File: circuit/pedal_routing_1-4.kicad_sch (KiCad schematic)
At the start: 4 parts, among them U110 CD4051B, U113 CD4051B, U114 CD4051B, U116 CD4051B

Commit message: Rebuilt bus and matrix.
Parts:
- renumbered U110 to U16, U114 to U17, U113 to U18, U116 to U19
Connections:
- net AGND: no longer U16.4 (X7), U17.4 (X7), U18.4 (X7), U19.4 (X7)
- net Guitar_Out renamed ROW_2
- net Pedal1_Out renamed ROW_3
- net ROW_3: now also U16.15 (X2); no longer U16.13 (X0)
- net Pedal2_Out renamed ROW_4
- net ROW_4: now also U16.12 (X3), U17.12 (X3); no longer U16.15 (X2), U17.13 (X0)
- removed net Pedal3_Out: U16.12 (X3), U17.12 (X3), U18.13 (X0), U19.1 (X4)
- net Pedal4_Out renamed ROW_5
- net ROW_5: now also U19.1 (X4); no longer U19.13 (X0)
- net Pedal7_Out renamed ROW_6
- net Pedal8_Out renamed ROW_7
- net Row2 renamed PEDAL_1_IN
- net Row3 renamed PEDAL_2_IN
- net Row4 renamed PEDAL_3_IN
- net Row5 renamed PEDAL_4_IN
- new net ROW_1: U16.13 (X0), U17.13 (X0), U18.13 (X0), U19.13 (X0)
- new net ROW_8: U16.4 (X7), U17.4 (X7), U18.4 (X7), U19.4 (X7)

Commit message: Hopefully close to finished
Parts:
- added C117, C118, C119, C120, C121, C122, C123, C124: 0.1mF, Capacitor_THT:C_Axial_L3.8mm_D2.6mm_P7.50mm_Horizontal, symbol Device:C_Small
- renumbered U16 to U17, U17 to U18, U18 to U19, U19 to U22
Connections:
- net U7_Q3 is gone; now on net U8_Q0: U17.11 (A)
- net U7_Q4 is gone; now on net U8_Q1: U17.10 (B)
- net U7_Q5 is gone; now on net U8_Q2: U17.9 (C)
- net U7_Q6 is gone; now on net U8_Q3: U18.11 (A)
- net U7_Q7 is gone; now on net U8_Q4: U18.10 (B)
- net +5V: now also C118.2, C120.2, C122.2, C124.2
- net -5V: now also C117.1, C119.1, C121.1, C123.1
- net AGND: now also C117.2, C118.1, C119.2, C120.1, C121.2, C122.1, C123.2, C124.1
- net U8_Q0: no longer U18.9 (C)
- net U8_Q1: no longer U19.11 (A)
- net U8_Q2: no longer U19.10 (B)
- net U8_Q3: no longer U19.9 (C)
- net U8_Q4: no longer U22.11 (A)
- net U8_Q5: now also U18.9 (C); no longer U22.10 (B)
- net U8_Q6: now also U19.11 (A); no longer U22.9 (C)
- net ROW_8 renamed ROW_9
- new net U8_Q7: U19.10 (B)
- new net U9_Q0: U19.9 (C)
- new net U9_Q1: U22.11 (A)
- new net U9_Q2: U22.10 (B)
- new net U9_Q3: U22.9 (C)
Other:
- moved on the sheet: U17, U18, U19

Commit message: Created pdf and made minor readabilty changes.
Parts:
- C117, C118, C119, C120, C121, C122, C123, C124: value 0.1mF -> 0.1uF
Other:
- title: (none) -> ESP332 Guitar Patch Bay
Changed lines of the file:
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@@
 	(generator "eeschema")
 	(generator_version "9.0")
-	(paper "A4")
+	(paper "USLetter")
+	(title_block
+		(title "ESP332 Guitar Patch Bay")
+		(date "2025-05-27")
+		(rev "1")
+	)
 	(text "Pedal 2 Routing"
 		(exclude_from_sim no)
@@
 			)
 		)
-		(property "Value" "0.1mF"
+		(property "Value" "0.1uF"
 			(at 166.3636 31.75 90)
 			(effects
@@
 			)
 		)
-		(property "Value" "0.1mF"
+		(property "Value" "0.1uF"
 			(at 142.2336 80.01 90)
 			(effects
@@
 			)
 		)
-		(property "Value" "0.1mF"
+		(property "Value" "0.1uF"
 			(at 120.6436 118.11 90)
 			(effects
@@
 			)
 		)
-		(property "Value" "0.1mF"
+		(property "Value" "0.1uF"
 			(at 59.6836 80.01 90)
 			(effects
@@
 			)
 		)
-		(property "Value" "0.1mF"
+		(property "Value" "0.1uF"
 			(at 81.2736 33.02 90)
 			(effects
@@
 			)
 		)
-		(property "Value" "0.1mF"
+		(property "Value" "0.1uF"
 			(at 96.5136 165.1 90)
 			(effects
@@
 			)
 		)
-		(property "Value" "0.1mF"
+		(property "Value" "0.1uF"
 			(at 242.5636 30.48 90)
 			(effects
@@
 			)
 		)
-		(property "Value" "0.1mF"
+		(property "Value" "0.1uF"
 			(at 212.0836 77.47 90)
 			(effects

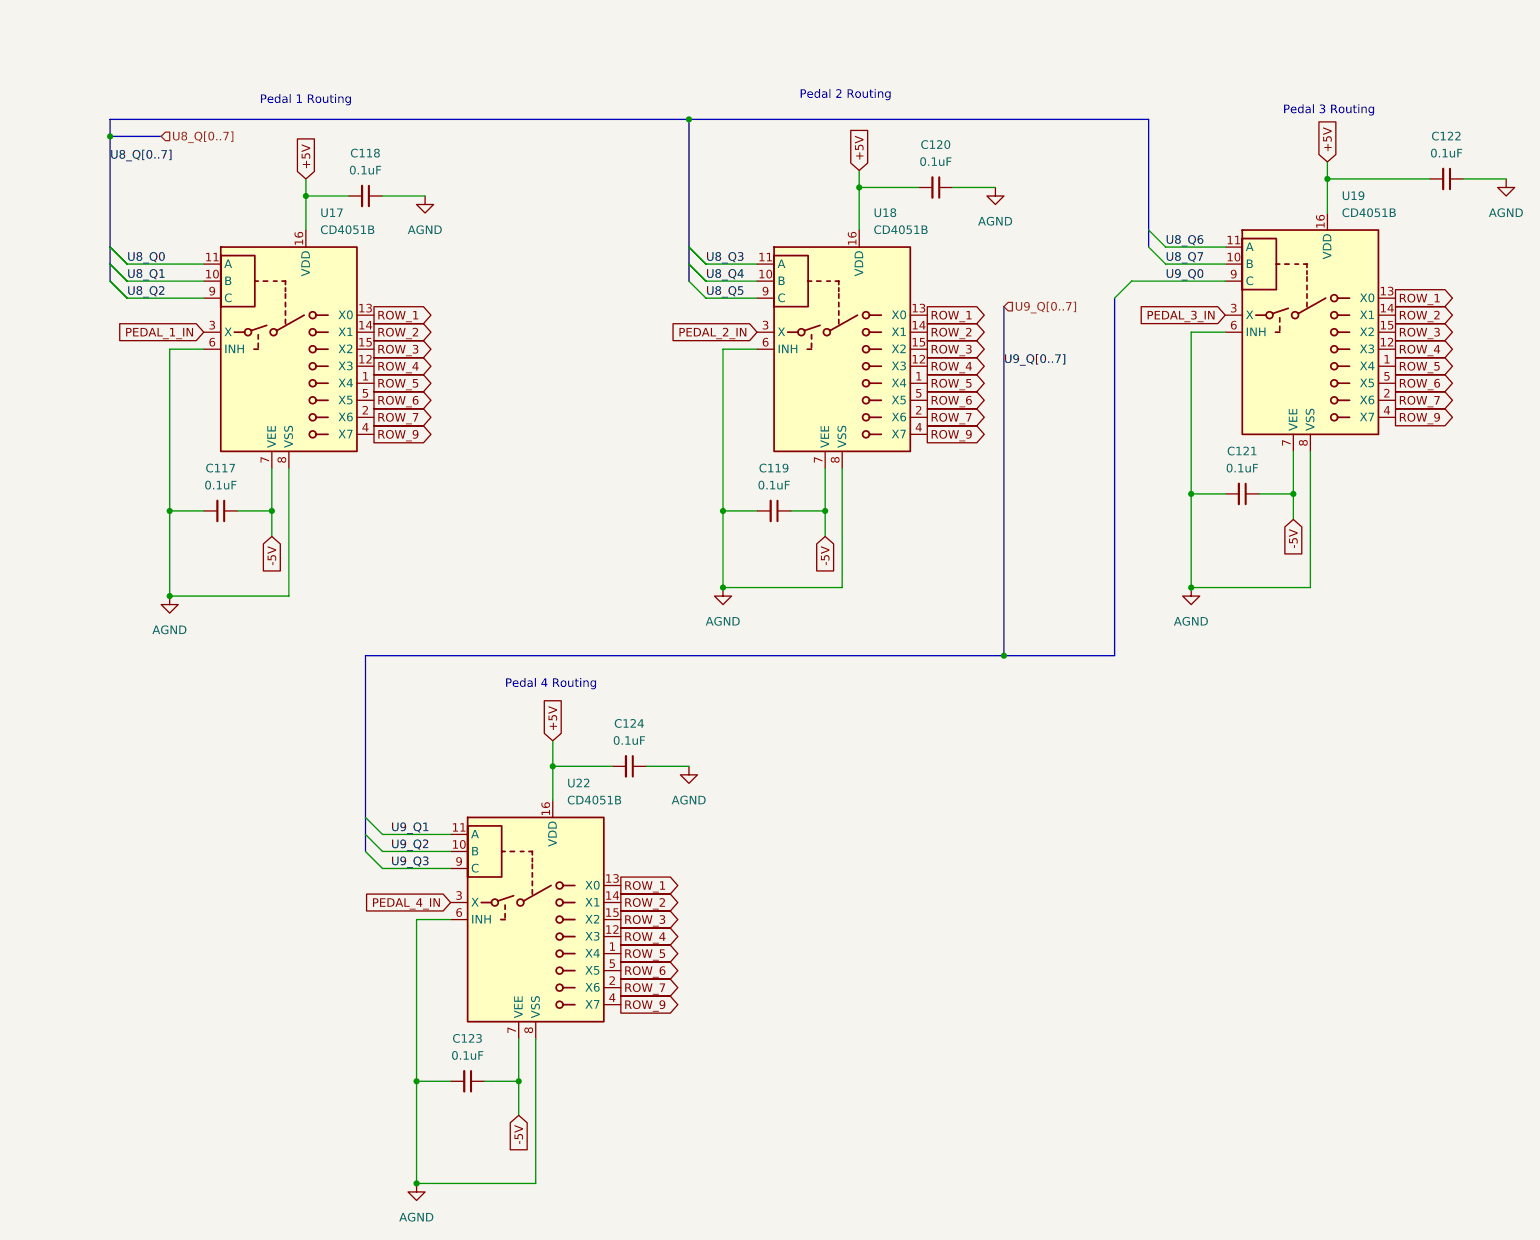
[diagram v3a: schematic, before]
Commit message: Rebuilt Matrix and added inhibit function.
Matrix was flawed, It now supports 8 FX loops (pedals) in any order. Or optionally none at all with a buffered bypass, or anywhere in between. The inhibit function will allow the option to press any loop foot switch an enable or disable it without reprogramming.
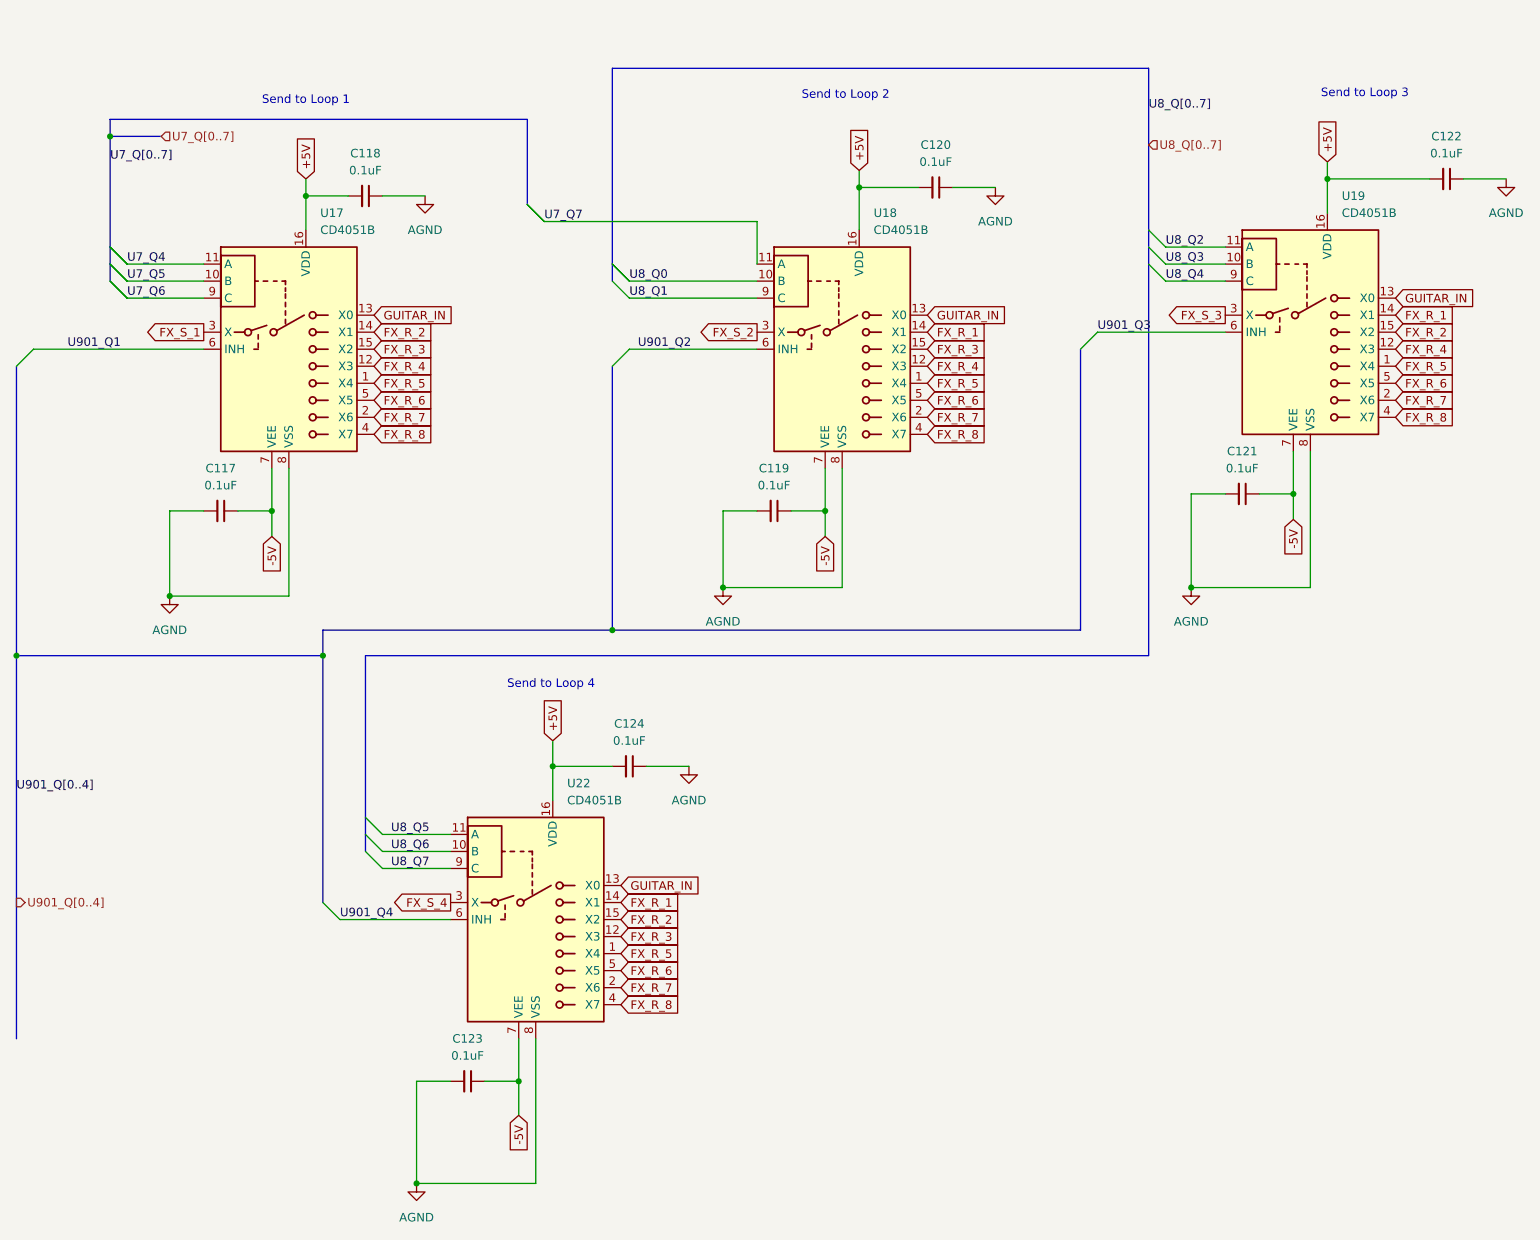
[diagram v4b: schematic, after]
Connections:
- net U9_Q0 is gone; now on net U8_Q4: U19.9 (C)
- net U9_Q1 is gone; now on net U8_Q5: U22.11 (A)
- net U9_Q2 is gone; now on net U8_Q6: U22.10 (B)
- net U9_Q3 is gone; now on net U8_Q7: U22.9 (C)
- net AGND: no longer U17.6 (INH), U18.6 (INH), U19.6 (INH), U22.6 (INH)
- net U8_Q0: now also U18.10 (B); no longer U17.11 (A)
- net U8_Q1: now also U18.9 (C); no longer U17.10 (B)
- net U8_Q2: now also U19.11 (A); no longer U17.9 (C)
- net U8_Q3: now also U19.10 (B); no longer U18.11 (A)
- net U8_Q4: no longer U18.10 (B)
- net U8_Q5: no longer U18.9 (C)
- net U8_Q6: no longer U19.11 (A)
- net U8_Q7: no longer U19.10 (B)
- net PEDAL_1_IN renamed FX_S_1
- net PEDAL_2_IN renamed FX_S_2
- net PEDAL_3_IN renamed FX_S_3
- net PEDAL_4_IN renamed FX_S_4
- net ROW_1 renamed GUITAR_IN
- net ROW_2 renamed FX_R_1
- net FX_R_1: no longer U17.14 (X1)
- net ROW_3 renamed FX_R_2
- net FX_R_2: now also U17.14 (X1); no longer U17.15 (X2), U18.15 (X2)
- net ROW_4 renamed FX_R_4
- net FX_R_4: no longer U22.12 (X3)
- net ROW_5 renamed FX_R_5
- net ROW_6 renamed FX_R_6
- net ROW_7 renamed FX_R_7
- net ROW_9 renamed FX_R_8
- new net FX_R_3: U17.15 (X2), U18.15 (X2), U22.12 (X3)
- new net U7_Q4: U17.11 (A)
- new net U7_Q5: U17.10 (B)
- new net U7_Q6: U17.9 (C)
- new net U7_Q7: U18.11 (A)
- new net U901_Q1: U17.6 (INH)
- new net U901_Q2: U18.6 (INH)
- new net U901_Q3: U19.6 (INH)
- new net U901_Q4: U22.6 (INH)
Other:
- note added: "Send to Loop 1"
- note added: "Send to Loop 2"
- note added: "Send to Loop 3"
- note added: "Send to Loop 4"
- note removed: "Pedal 1 Routing"
- note removed: "Pedal 2 Routing"
- note removed: "Pedal 3 Routing"
- note removed: "Pedal 4 Routing"

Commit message: Re-annotation of circuit, new PCB routing, updated PDF
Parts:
- renumbered C122 to C501, C120 to C502, C118 to C503, C121 to C504, C117 to C505, C119 to C506, C124 to C507, C123 to C508, U19 to U501, U17 to U502, U18 to U503, U22 to U504
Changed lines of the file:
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@@
 		(on_board yes)
 		(dnp no)
-		(property "Reference" "#PWR0503"
+		(property "Reference" "#PWR0506"
 			(at 52.07 102.87 0)
 			(effects
@@
 			(project "circuit"
 				(path "/420e3d7a-6c9a-4806-b4be-05d56aeb21de/be7f89fe-51f3-4dfc-9362-b897b38bc33a"
-					(reference "#PWR0503")
+					(reference "#PWR0506")
 					(unit 1)
 				)
@@
 		(on_board yes)
 		(dnp no)
-		(property "Reference" "#PWR0508"
+		(property "Reference" "#PWR0507"
 			(at 129.54 128.27 0)
 			(effects
@@
 			(project "circuit"
 				(path "/420e3d7a-6c9a-4806-b4be-05d56aeb21de/be7f89fe-51f3-4dfc-9362-b897b38bc33a"
-					(reference "#PWR0508")
+					(reference "#PWR0507")
 					(unit 1)
 				)
@@
 		(on_board yes)
 		(dnp no)
-		(property "Reference" "#PWR0505"
+		(property "Reference" "#PWR0502"
 			(at 175.26 41.91 0)
 			(effects
@@
 			(project "circuit"
 				(path "/420e3d7a-6c9a-4806-b4be-05d56aeb21de/be7f89fe-51f3-4dfc-9362-b897b38bc33a"
-					(reference "#PWR0505")
+					(reference "#PWR0502")
 					(unit 1)
 				)
@@
 		(dnp no)
 		(fields_autoplaced yes)
-		(property "Reference" "U19"
+		(property "Reference" "U501"
 			(at 226.9333 36.83 0)
 			(effects
@@
 			(project "circuit"
 				(path "/420e3d7a-6c9a-4806-b4be-05d56aeb21de/be7f89fe-51f3-4dfc-9362-b897b38bc33a"
-					(reference "U19")
+					(reference "U501")
 					(unit 1)
 				)
@@
 		(on_board yes)
 		(dnp no)
-		(property "Reference" "#PWR0501"
+		(property "Reference" "#PWR0504"
 			(at 134.62 101.6 0)
 			(effects
@@
 			(project "circuit"
 				(path "/420e3d7a-6c9a-4806-b4be-05d56aeb21de/be7f89fe-51f3-4dfc-9362-b897b38bc33a"
-					(reference "#PWR0501")
+					(reference "#PWR0504")
 					(unit 1)
 				)
@@
 		(dnp no)
 		(fields_autoplaced yes)
-		(property "Reference" "C120"
+		(property "Reference" "C502"
 			(at 166.3636 29.21 90)
 			(effects
@@
 			(project "circuit"
 				(path "/420e3d7a-6c9a-4806-b4be-05d56aeb21de/be7f89fe-51f3-4dfc-9362-b897b38bc33a"
-					(reference "C120")
+					(reference "C502")
 					(unit 1)
 				)
@@
 		(dnp no)
 		(fields_autoplaced yes)
-		(property "Reference" "U18"
+		(property "Reference" "U503"
 			(at 157.0833 39.37 0)
 			(effects
@@
 			(project "circuit"
 				(path "/420e3d7a-6c9a-4806-b4be-05d56aeb21de/be7f89fe-51f3-4dfc-9362-b897b38bc33a"
-					(reference "U18")
+					(reference "U503")
 					(unit 1)
 				)
@@
 		(on_board yes)
 		(dnp no)
-		(property "Reference" "#PWR0506"
+		(property "Reference" "#PWR0503"
 			(at 90.17 43.18 0)
 			(effects
@@
 			(project "circuit"
 				(path "/420e3d7a-6c9a-4806-b4be-05d56aeb21de/be7f89fe-51f3-4dfc-9362-b897b38bc33a"
-					(reference "#PWR0506")
+					(reference "#PWR0503")
 					(unit 1)
 				)
@@
 		(on_board yes)
 		(dnp no)
-		(property "Reference" "#PWR0504"
+		(property "Reference" "#PWR0508"
 			(at 88.9 190.5 0)
 			(effects
@@
 			(project "circuit"
 				(path "/420e3d7a-6c9a-4806-b4be-05d56aeb21de/be7f89fe-51f3-4dfc-9362-b897b38bc33a"
-					(reference "#PWR0504")
+					(reference "#PWR0508")
 					(unit 1)
 				)
@@
 		(dnp no)
 		(fields_autoplaced yes)
-		(property "Reference" "C119"
+		(property "Reference" "C506"
 			(at 142.2336 77.47 90)
 			(effects
@@
 			(project "circuit"
 				(path "/420e3d7a-6c9a-4806-b4be-05d56aeb21de/be7f89fe-51f3-4dfc-9362-b897b38bc33a"
-					(reference "C119")
+					(reference "C506")
 					(unit 1)
 				)
@@
 		(on_board yes)
 		(dnp no)
-		(property "Reference" "#PWR0502"
+		(property "Reference" "#PWR0505"
 			(at 204.47 101.6 0)
 			(effects
@@
 			(project "circuit"
 				(path "/420e3d7a-6c9a-4806-b4be-05d56aeb21de/be7f89fe-51f3-4dfc-9362-b897b38bc33a"
-					(reference "#PWR0502")
+					(reference "#PWR0505")
 					(unit 1)
 				)
@@
 		(on_board yes)
 		(dnp no)
-		(property "Reference" "#PWR0507"
+		(property "Reference" "#PWR0501"
 			(at 251.46 40.64 0)
 			(effects
@@
 			(project "circuit"
 				(path "/420e3d7a-6c9a-4806-b4be-05d56aeb21de/be7f89fe-51f3-4dfc-9362-b897b38bc33a"
-					(reference "#PWR0507")
+					(reference "#PWR0501")
 					(unit 1)
 				)
@@
 		(dnp no)
 		(fields_autoplaced yes)
-		(property "Reference" "U17"
+		(property "Reference" "U502"
 			(at 74.5333 39.37 0)
 			(effects
@@
 			(project "circuit"
 				(path "/420e3d7a-6c9a-4806-b4be-05d56aeb21de/be7f89fe-51f3-4dfc-9362-b897b38bc33a"
-					(reference "U17")
+					(reference "U502")
 					(unit 1)
 				)
@@
 		(dnp no)
 		(fields_autoplaced yes)
-		(property "Reference" "C124"
+		(property "Reference" "C507"
 			(at 120.6436 115.57 90)
 			(effects
@@
 			(project "circuit"
 				(path "/420e3d7a-6c9a-4806-b4be-05d56aeb21de/be7f89fe-51f3-4dfc-9362-b897b38bc33a"
-					(reference "C124")
+					(reference "C507")
 					(unit 1)
 				)
@@
 		(on_board yes)
 		(dnp no)
-		(property "Reference" "U22"
+		(property "Reference" "U504"
 			(at 111.3633 124.46 0)
 			(effects
@@
 			(project "circuit"
 				(path "/420e3d7a-6c9a-4806-b4be-05d56aeb21de/be7f89fe-51f3-4dfc-9362-b897b38bc33a"
-					(reference "U22")
+					(reference "U504")
 					(unit 1)
 				)
@@
 		(dnp no)
 		(fields_autoplaced yes)
-		(property "Reference" "C117"
+		(property "Reference" "C505"
 			(at 59.6836 77.47 90)
 			(effects
@@
 			(project ""
 				(path "/420e3d7a-6c9a-4806-b4be-05d56aeb21de/be7f89fe-51f3-4dfc-9362-b897b38bc33a"
-					(reference "C117")
+					(reference "C505")
 					(unit 1)
 				)
@@
 		(dnp no)
 		(fields_autoplaced yes)
-		(property "Reference" "C118"
+		(property "Reference" "C503"
 			(at 81.2736 30.48 90)
 			(effects
@@
 			(project "circuit"
 				(path "/420e3d7a-6c9a-4806-b4be-05d56aeb21de/be7f89fe-51f3-4dfc-9362-b897b38bc33a"
-					(reference "C118")
+					(reference "C503")
 					(unit 1)
 				)
@@
 		(dnp no)
 		(fields_autoplaced yes)
-		(property "Reference" "C123"
+		(property "Reference" "C508"
 			(at 96.5136 162.56 90)
 			(effects
@@
 			(project "circuit"
 				(path "/420e3d7a-6c9a-4806-b4be-05d56aeb21de/be7f89fe-51f3-4dfc-9362-b897b38bc33a"
-					(reference "C123")
+					(reference "C508")
 					(unit 1)
 				)
@@
 		(dnp no)
 		(fields_autoplaced yes)
-		(property "Reference" "C122"
+		(property "Reference" "C501"
 			(at 242.5636 27.94 90)
 			(effects
@@
 			(project "circuit"
 				(path "/420e3d7a-6c9a-4806-b4be-05d56aeb21de/be7f89fe-51f3-4dfc-9362-b897b38bc33a"
-					(reference "C122")
+					(reference "C501")
 					(unit 1)
 				)
@@
 		(dnp no)
 		(fields_autoplaced yes)
-		(property "Reference" "C121"
+		(property "Reference" "C504"
 			(at 212.0836 74.93 90)
 			(effects
@@
 			(project "circuit"
 				(path "/420e3d7a-6c9a-4806-b4be-05d56aeb21de/be7f89fe-51f3-4dfc-9362-b897b38bc33a"
-					(reference "C121")
-					(unit 1)
-				)
+					(reference "C504")
+					(unit 1)
+				)
